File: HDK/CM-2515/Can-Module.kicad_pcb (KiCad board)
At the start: 2 copper layers, 34.5 x 14.2 mm, 13 parts, among them J101 Can Connect, J102 Can Connect, SW101 SW_DIP_x01, U101 SN65HVD230, U102 MCP2515-xST, Y101 8MHz

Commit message: added fd module
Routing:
- net /~{CS}: track 10.1 -> 12.5 mm
- net GND: vias 5 -> 15
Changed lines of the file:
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@@
   (segment (start 124.947 114.791) (end 123.417 114.791) (width 0.25) (layer "F.Cu") (net 2))
   (via (at 124.697 116.411) (size 0.8) (drill 0.4) (layers "F.Cu" "B.Cu") (net 2))
+  (via (at 131.4 121) (size 0.8) (drill 0.4) (layers "F.Cu" "B.Cu") (free) (net 2))
+  (via (at 135.8 108.4) (size 0.8) (drill 0.4) (layers "F.Cu" "B.Cu") (free) (net 2))
+  (via (at 111.2 120.8) (size 0.8) (drill 0.4) (layers "F.Cu" "B.Cu") (free) (net 2))
+  (via (at 117.8 118.6) (size 0.8) (drill 0.4) (layers "F.Cu" "B.Cu") (free) (net 2))
+  (via (at 125.4 108.4) (size 0.8) (drill 0.4) (layers "F.Cu" "B.Cu") (free) (net 2))
   (via (at 119.997 110.736) (size 0.8) (drill 0.4) (layers "F.Cu" "B.Cu") (net 2))
   (via (at 114.057 119.411) (size 0.8) (drill 0.4) (layers "F.Cu" "B.Cu") (net 2))
+  (via (at 127.8 114.8) (size 0.8) (drill 0.4) (layers "F.Cu" "B.Cu") (free) (net 2))
+  (via (at 122.2 110.6) (size 0.8) (drill 0.4) (layers "F.Cu" "B.Cu") (free) (net 2))
   (via (at 123.997 111.511) (size 0.8) (drill 0.4) (layers "F.Cu" "B.Cu") (net 2))
+  (via (at 122.8 108.4) (size 0.8) (drill 0.4) (layers "F.Cu" "B.Cu") (free) (net 2))
   (via (at 119.795714 112.560116) (size 0.8) (drill 0.4) (layers "F.Cu" "B.Cu") (net 2))
+  (via (at 126.8 119.2) (size 0.8) (drill 0.4) (layers "F.Cu" "B.Cu") (free) (net 2))
+  (via (at 110.4 108.8) (size 0.8) (drill 0.4) (layers "F.Cu" "B.Cu") (free) (net 2))
   (segment (start 112.517 119.793) (end 113.041 120.317) (width 0.4) (layer "F.Cu") (net 3))
   (segment (start 112.517 118.311) (end 112.517 119.793) (width 0.4) (layer "F.Cu") (net 3))
@@
   (segment (start 113.372 115.736) (end 112.2345 115.736) (width 0.25) (layer "F.Cu") (net 22))
   (via (at 113.997 115.111) (size 0.8) (drill 0.4) (layers "F.Cu" "B.Cu") (net 22))
-  (segment (start 113.997 115.111) (end 113.597 115.111) (width 0.25) (layer "B.Cu") (net 22))
-  (segment (start 113.597 115.111) (end 108.197 109.711) (width 0.25) (layer "B.Cu") (net 22))
+  (segment (start 113.997 110.997) (end 112.711 109.711) (width 0.25) (layer "B.Cu") (net 22))
+  (segment (start 112.711 109.711) (end 108.197 109.711) (width 0.25) (layer "B.Cu") (net 22))
+  (segment (start 113.997 115.111) (end 113.997 110.997) (width 0.25) (layer "B.Cu") (net 22))
   (segment (start 115.797 117.711) (end 115.797 118.311) (width 0.25) (layer "F.Cu") (net 23))
   (segment (start 112.2345 116.386) (end 114.472 116.386) (width 0.25) (layer "F.Cu") (net 23))

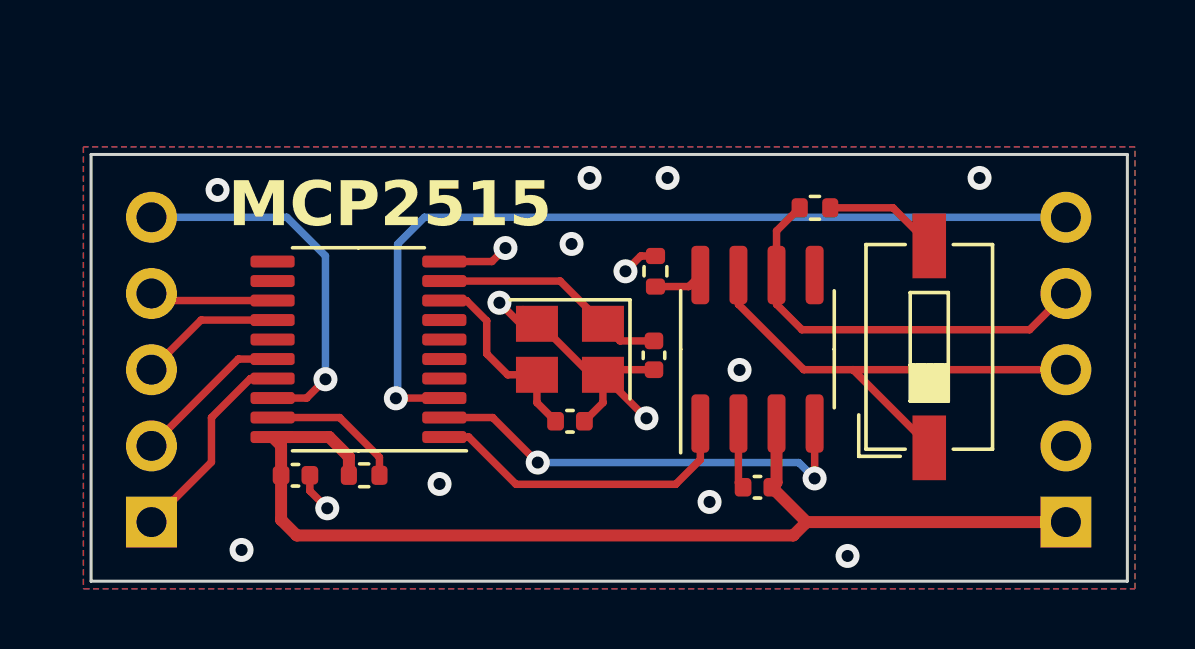
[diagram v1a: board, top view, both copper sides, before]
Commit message: updated CM2515
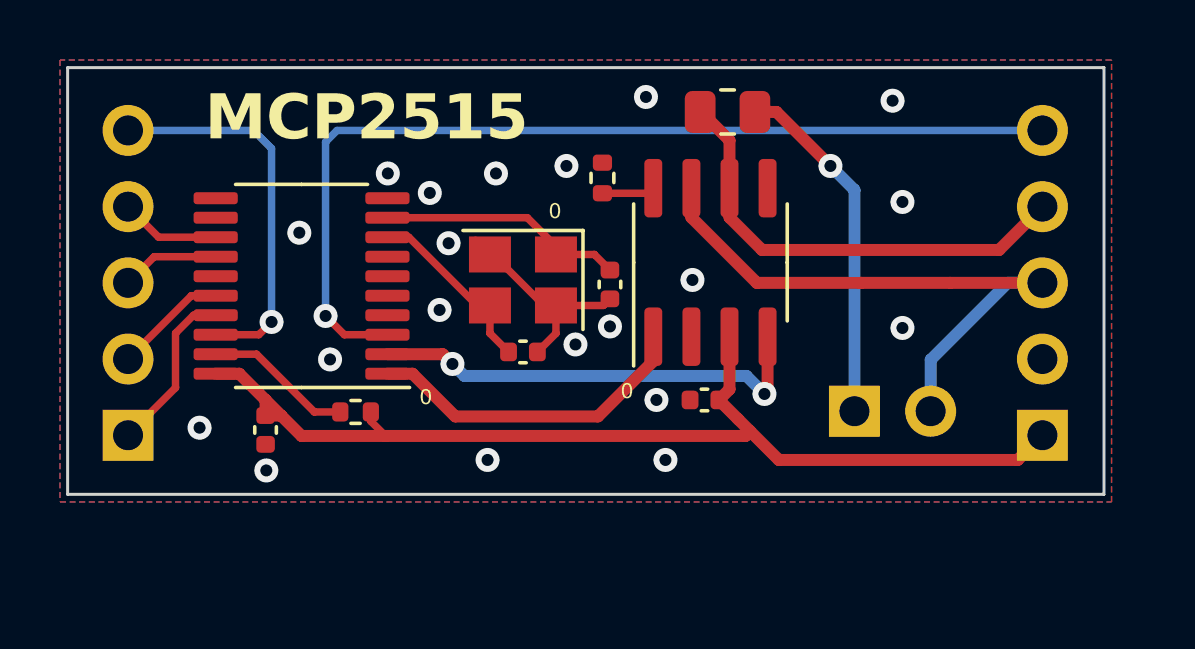
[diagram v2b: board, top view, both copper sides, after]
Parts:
- removed SW101: SW_DIP_x01, Button_Switch_SMD:SW_DIP_SPSTx01_Slide_6.7x4.1mm_W6.73mm_P2.54mm_LowProfile_JPin
- added J103: Can Termination, NVF-Kicad:PinHeader_1x02_P2.54mm_Horizontal, F.Cu at (131.6, 116.2)
- C103, C104: value 10p -> 20p
- R103: footprint Resistor_SMD:R_0402_1005Metric -> Resistor_SMD:R_0805_2012Metric
- Y101: value 8MHz -> 40MHz
- moved R103 4.32 mm to (127.4, 106.2)
- moved R101 3.58 mm to (123.2, 108.4)
- moved C102 3.41 mm to (126.6, 115.8)
- moved U101 3.29 mm to (126.8, 111.2)
- moved J101 3.00 mm to (107.4, 117.0)
- moved J102 3.00 mm to (137.9, 117.0)
- moved U102 2.84 mm to (113.2, 112.0)
- moved Y101 2.79 mm to (120.6, 111.8)
- moved C104 2.79 mm to (120.6, 114.2)
- moved C103 2.78 mm to (123.5, 112.0)
- moved R102 2.13 mm to (115.0, 116.2), turned to 0 degrees
- moved C101 1.81 mm to (112.0, 116.8), turned to -90 degrees
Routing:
- net GND: track 17.7 -> 8.06 mm, vias 15 -> 20
- net Net-(J103-Pin_1): track 3.80 -> 11.7 mm, vias 0 -> 1
- net /CAN_H: track 16.4 -> 20.1 mm
- net /SOF: track 29.4 -> 32.2 mm
- net +3V3: track 36.7 -> 35.0 mm
- net /SPI_SCK: track 4.72 -> 3.28 mm
- net /SPI_MOSI: track 5.24 -> 3.80 mm
- net /CAN_L: track 14.0 -> 15.4 mm
- net /SPI_MISO: track 6.89 -> 5.64 mm
- net /CAN_IRQ: track 4.13 -> 3.34 mm
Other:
- board text added: "0"
